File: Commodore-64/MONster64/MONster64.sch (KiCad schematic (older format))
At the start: 90 parts, among them J1 USB Power, J10 USB_B_Micro, J11 Hirose_DM3D-SF, J12 Conn_01x20, J13 RJ45_Amphenol_RJMG1BD3B8K1ANR, J2 CLOCK_JUMPER, J3 3v3, J4 4pin Expansion, J5 Conn_01x20, J6 GND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

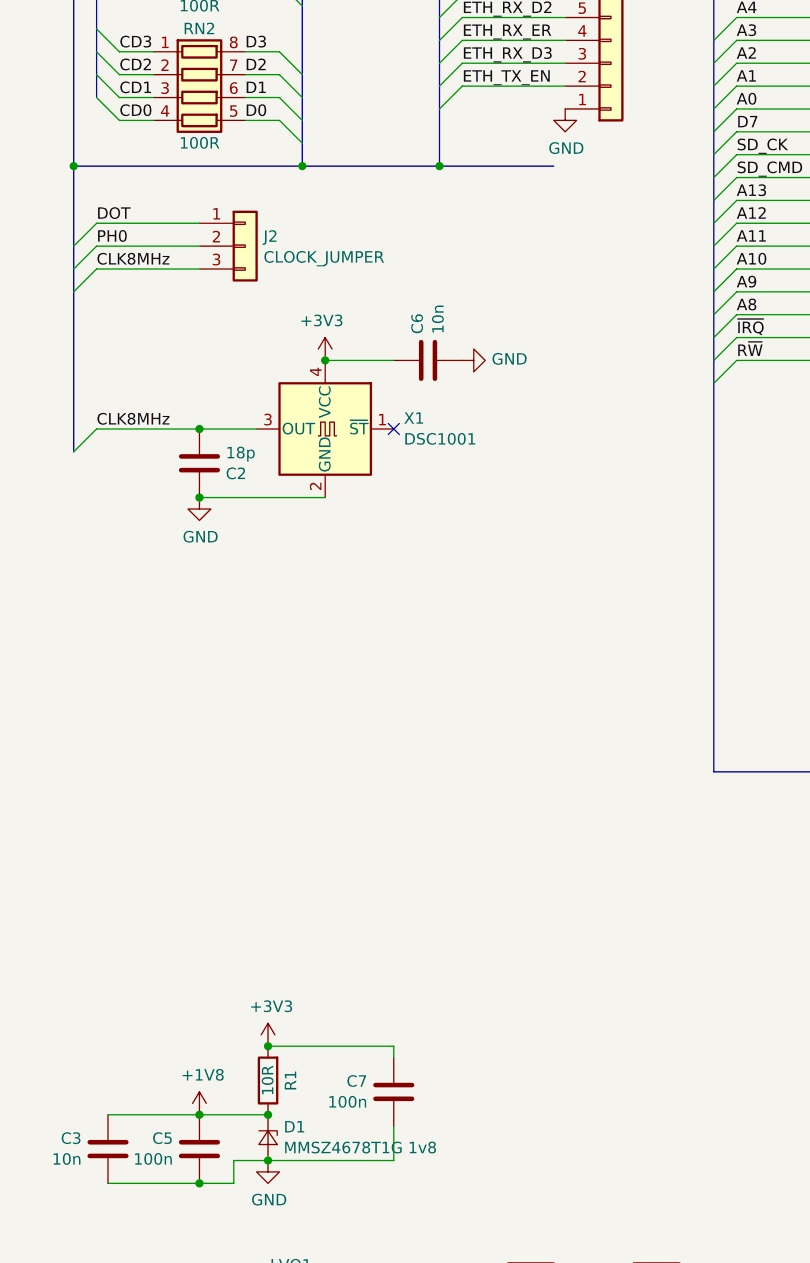
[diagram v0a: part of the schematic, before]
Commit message: zener tweak
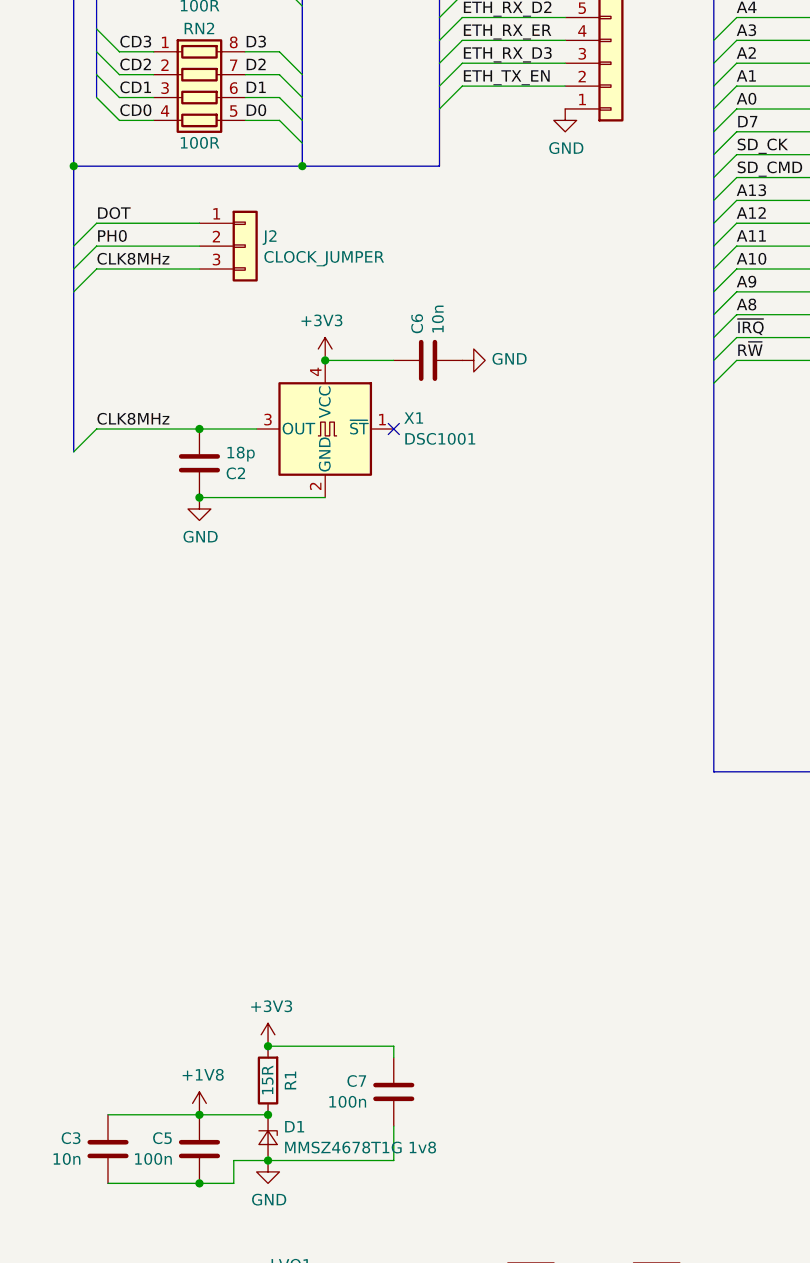
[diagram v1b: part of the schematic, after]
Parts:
- R1: value 10R -> 15R
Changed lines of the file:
@@
 Entry Wire Line
 	950  5850 1050 5750
-Wire Bus Line
-	3050 5500 2550 5500
-Connection ~ 2550 5500
 Text Label 3850 3850 0    50   ~ 0
 NF_IO0
@@
 P 1800 9500
 F 0 "R1" V 1700 9500 50  0000 C CNN
-F 1 "10R" V 1800 9500 50  0000 C CNN
+F 1 "15R" V 1800 9500 50  0000 C CNN
 F 2 "Resistor_SMD:R_0805_2012Metric_Pad1.15x1.40mm_HandSolder" V 1730 9500 50  0001 C CNN
 F 3 "~" H 1800 9500 50  0001 C CNN

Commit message: Add files via upload
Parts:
- removed D1: MMSZ4678T1G 1v8, Diode_SMD:D_SOD-123, symbol Device:D_Zener_Small
- removed LVO1: NCP1117LPST33T3G, Package_TO_SOT_SMD:SOT-223-3_TabPin2, symbol Regulator_Linear:AMS1117-3.3
- removed R1: 15R, Resistor_SMD:R_0805_2012Metric_Pad1.15x1.40mm_HandSolder, symbol Device:R
- added C45: 100n, Capacitor_SMD:C_0805_2012Metric_Pad1.15x1.40mm_HandSolder, symbol Device:C
- added U5: SN74AUP1T34DCK, Package_TO_SOT_SMD:SOT-353_SC-70-5, symbol Logic_LevelTranslator:SN74AUP1T34DCK
- added U6: MIC5356-SGYMME, Package_SO:MSOP-8-1EP_3x3mm_P0.65mm_EP2.5x3mm_Mask1.73x2.36mm_ThermalVias, symbol CPU2:MIC5356-SGYMME
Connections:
- net +1V8: now also U6.6 (OUT1)
- net +3V3: now also C45.1, U5.5 (VCCB), U6.1 (OUT2); no longer J9.2 (Pin_2)
- net +5V: now also J9.2 (Pin_2), U6.3 (EN2), U6.4 (EN1), U6.5 (IN)
- net DOT: now also U5.2 (A); no longer J2.1 (Pin_1)
- net GND: now also C45.2, U5.3 (GND), U6.2 (GND), U6.9 (GND)
- new net DOT_3v3: J2.1 (Pin_1), U5.4 (B)
- no-connect marks 3 -> 4
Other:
- moved on the sheet: C3, C5, C7

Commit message: Add files via upload
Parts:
- removed U6: MIC5356-SGYMME, Package_SO:MSOP-8-1EP_3x3mm_P0.65mm_EP2.5x3mm_Mask1.73x2.36mm_ThermalVias, symbol CPU2:MIC5356-SGYMME
- added U6: MIC5356-SGYMME, Package_SO:MSOP-8-1EP_3x3mm_P0.65mm_EP2.5x3mm_Mask1.73x2.36mm_ThermalVias, symbol Regulator_Linear:MIC5356-SGYMME
- U1: value STM32H753VIT6 -> STM32H743VIT6
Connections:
- net +1V8: now also U6.7 (VOUT2)
- net +3V3: now also U6.8 (VOUT1)
- net +5V: now also U6.1 (VIN)
- net GND: now also U6.2 (GND), U6.9 (GND)
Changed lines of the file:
@@
 F 1 "100R" V 1700 4600 50  0000 C CNN
 F 2 "Resistor_SMD:R_Array_Convex_4x1206" V 1775 4600 50  0001 C CNN
-F 3 "~" H 1500 4600 50  0001 C CNN
+F 3 "YC324-JK-07100RL" H 1500 4600 50  0001 C CNN
 	1    1500 4600
 	0    1    1    0
@@
 F 1 "100R" V 1700 5200 50  0000 C CNN
 F 2 "Resistor_SMD:R_Array_Convex_4x1206" V 1775 5200 50  0001 C CNN
-F 3 "~" H 1500 5200 50  0001 C CNN
+F 3 "YC324-JK-07100RL" H 1500 5200 50  0001 C CNN
 	1    1500 5200
 	0    1    1    0
@@
 P 5200 3850
 F 0 "U1" H 5600 1050 50  0000 C CNN
-F 1 "STM32H753VIT6" H 5800 1200 50  0000 C CNN
+F 1 "STM32H743VIT6" H 5800 1200 50  0000 C CNN
 F 2 "Package_QFP:LQFP-100_14x14mm_P0.5mm" H 4500 1250 50  0001 R CNN
 F 3 "http://www.st.com/st-web-ui/static/active/en/resource/technical/document/datasheet/DM00388325.pdf" H 5200 3850 50  0001 C CNN
@@
 L power:+3V3 #PWR0104
 U 1 1 5F554FF3
-P 3300 9550
-F 0 "#PWR0104" H 3300 9400 50  0001 C CNN
-F 1 "+3V3" H 3315 9723 50  0000 C CNN
-F 2 "" H 3300 9550 50  0001 C CNN
-F 3 "" H 3300 9550 50  0001 C CNN
-	1    3300 9550
+P 3300 9600
+F 0 "#PWR0104" H 3300 9450 50  0001 C CNN
+F 1 "+3V3" H 3315 9773 50  0000 C CNN
+F 2 "" H 3300 9600 50  0001 C CNN
+F 3 "" H 3300 9600 50  0001 C CNN
+	1    3300 9600
 	1    0    0    -1
 $EndComp
@@
 $EndComp
 Wire Wire Line
-	3200 9550 3300 9550
+	3200 9600 3300 9600
 Wire Wire Line
 	3200 9700 3450 9700
@@
 	2700 7850 2700 7700
 Connection ~ 1900 7850
-Wire Wire Line
-	2400 9500 2400 9600
 $Comp
-L CPU2:MIC5356-SGYMME U6
-U 1 1 5F279463
+L Regulator_Linear:MIC5356-SGYMME U6
+U 1 1 5F5B1677
 P 2800 9600
-F 0 "U6" H 2800 9967 50  0000 C CNN
-F 1 "MIC5356-SGYMME" H 2800 9876 50  0000 C CNN
+F 0 "U6" H 2800 9981 50  0000 C CNN
+F 1 "MIC5356-SGYMME" H 2800 9890 50  0000 C CNN
 F 2 "Package_SO:MSOP-8-1EP_3x3mm_P0.65mm_EP2.5x3mm_Mask1.73x2.36mm_ThermalVias" H 4200 9350 50  0001 C CNN
 F 3 "http://ww1.microchip.com/downloads/en/DeviceDoc/mic5355_6.pdf" H 2800 9950 50  0001 C CNN
@@
 	1    0    0    -1
 $EndComp
-Connection ~ 2400 9500
-Wire Wire Line
-	2400 9600 2400 9700
 Wire Bus Line
 	950  5500 950  8250
@@
 Wire Bus Line
 	6650 800  6650 8150
-Connection ~ 2400 9600
 $EndSCHEMATC

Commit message: Add files via upload
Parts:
- RN1, RN2: footprint Resistor_SMD:R_Array_Convex_4x1206 -> Resistor_SMD:R_Array_Concave_4x0603
- U1: value STM32H743VIT6 -> STM32H753VIT6
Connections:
- no-connect marks 4 -> 6
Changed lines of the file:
@@
 Entry Wire Line
 	1050 3700 1150 3600
-$Comp
-L Device:R_Pack04 RN1
-U 1 1 5DA66EB2
-P 1500 4600
-F 0 "RN1" V 1200 4600 50  0000 C CNN
-F 1 "100R" V 1700 4600 50  0000 C CNN
-F 2 "Resistor_SMD:R_Array_Convex_4x1206" V 1775 4600 50  0001 C CNN
-F 3 "YC324-JK-07100RL" H 1500 4600 50  0001 C CNN
-	1    1500 4600
-	0    1    1    0
-$EndComp
 Entry Wire Line
 	1050 4300 1150 4400
@@
 Entry Wire Line
 	1050 4600 1150 4700
-$Comp
-L Device:R_Pack04 RN2
-U 1 1 5DA6909D
-P 1500 5200
-F 0 "RN2" V 1200 5200 50  0000 C CNN
-F 1 "100R" V 1700 5200 50  0000 C CNN
-F 2 "Resistor_SMD:R_Array_Convex_4x1206" V 1775 5200 50  0001 C CNN
-F 3 "YC324-JK-07100RL" H 1500 5200 50  0001 C CNN
-	1    1500 5200
-	0    1    1    0
-$EndComp
 Entry Wire Line
 	1050 4900 1150 5000
@@
 P 5200 3850
 F 0 "U1" H 5600 1050 50  0000 C CNN
-F 1 "STM32H743VIT6" H 5800 1200 50  0000 C CNN
+F 1 "STM32H753VIT6" H 5800 1200 50  0000 C CNN
 F 2 "Package_QFP:LQFP-100_14x14mm_P0.5mm" H 4500 1250 50  0001 R CNN
 F 3 "http://www.st.com/st-web-ui/static/active/en/resource/technical/document/datasheet/DM00388325.pdf" H 5200 3850 50  0001 C CNN
@@
 	1    0    0    -1
 $EndComp
+$Comp
+L Device:R_Pack04 RN1
+U 1 1 5F6D8CCD
+P 1500 4600
+F 0 "RN1" V 1200 4600 50  0000 C CNN
+F 1 "100R" V 1700 4600 50  0000 C CNN
+F 2 "Resistor_SMD:R_Array_Concave_4x0603" V 1775 4600 50  0001 C CNN
+F 3 "CAT16-101J4LF" H 1500 4600 50  0001 C CNN
+	1    1500 4600
+	0    1    1    0
+$EndComp
+$Comp
+L Device:R_Pack04 RN2
+U 1 1 5F7CB446
+P 1500 5200
+F 0 "RN2" V 1200 5200 50  0000 C CNN
+F 1 "100R" V 1700 5200 50  0000 C CNN
+F 2 "Resistor_SMD:R_Array_Concave_4x0603" V 1775 5200 50  0001 C CNN
+F 3 "CAT16-101J4LF" H 1500 5200 50  0001 C CNN
+	1    1500 5200
+	0    1    1    0
+$EndComp
+NoConn ~ 2400 9600
+NoConn ~ 2400 9700
 Wire Bus Line
 	950  5500 950  8250

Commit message: Add files via upload
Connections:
- net +5V: now also U6.4 (EN2), U6.5 (EN1)
- no-connect marks 6 -> 4
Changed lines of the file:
@@
 	0    1    1    0
 $EndComp
-NoConn ~ 2400 9600
-NoConn ~ 2400 9700
+Wire Wire Line
+	2400 9700 2400 9600
+Wire Wire Line
+	2400 9600 2400 9500
 Wire Bus Line
 	950  5500 950  8250
@@
 Wire Bus Line
 	6650 800  6650 8150
+Connection ~ 2400 9600
+Connection ~ 2400 9500
 $EndSCHEMATC

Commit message: Add files via upload
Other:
- note added: "480MHz\n256MB RAM EXPANSION\nETHERNET/WIFI, USB, HDMI, YPbPr, VGA, TFT outputs? Sound device?\nCoprocessor w/ RNG, JPEG hardware compressor/decompressor (+DMA2D)\nCrypto, AI"
- note removed: "400MHz\n256MB RAM EXPANSION\nETHERNET/WIFI, USB\nHDMI, YPbPr, VGA, TFT outputs? Sound device?\nCoprocessor w/ RNG\nJPEG hardware compressor/decompressor (+DMA2D)"
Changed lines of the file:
@@
 $EndComp
 Text Notes 11850 10450 0    50   ~ 0
-400MHz\n256MB RAM EXPANSION\nETHERNET/WIFI, USB\nHDMI, YPbPr, VGA, TFT outputs? Sound device?\nCoprocessor w/ RNG\nJPEG hardware compressor/decompressor (+DMA2D)
+480MHz\n256MB RAM EXPANSION\nETHERNET/WIFI, USB, HDMI, YPbPr, VGA, TFT outputs? Sound device?\nCoprocessor w/ RNG, JPEG hardware compressor/decompressor (+DMA2D)\nCrypto, AI
 $Comp
 L Device:C C19
@@
 Wire Wire Line
 	2400 9600 2400 9500
+Connection ~ 2400 9600
+Connection ~ 2400 9500
 Wire Bus Line
 	950  5500 950  8250
@@
 Wire Bus Line
 	6650 800  6650 8150
-Connection ~ 2400 9600
-Connection ~ 2400 9500
 $EndSCHEMATC
